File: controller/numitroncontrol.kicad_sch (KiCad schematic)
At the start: 6 parts, among them J1 Conn_01x06, J2 Conn_01x06, J3 Conn_01x06

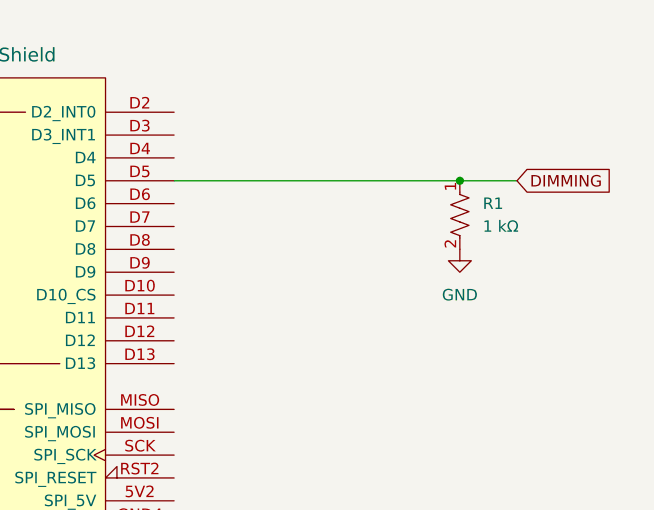
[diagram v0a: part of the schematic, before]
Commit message: arduino pinout
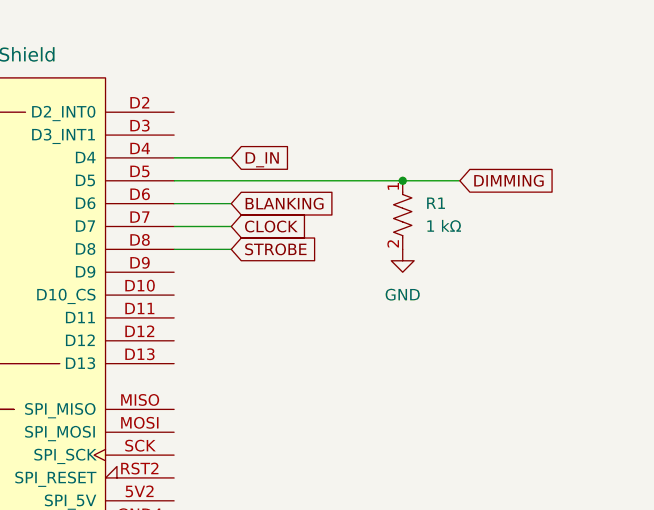
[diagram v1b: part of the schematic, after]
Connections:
- net BLANKING: now also A1.D6
- net CLOCK: now also A1.D7
- net D_IN: now also A1.D4
- net STROBE: now also A1.D8
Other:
- moved on the sheet: R1
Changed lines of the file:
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@@
 	)
 	(junction
-		(at 184.15 44.45)
+		(at 177.8 44.45)
 		(diameter 0)
 		(color 0 0 0 0)
@@
 	(wire
 		(pts
+			(xy 177.8 44.45) (xy 184.15 44.45)
+		)
+		(stroke
+			(width 0)
+			(type default)
+		)
+	)
+	(wire
+		(pts
 			(xy 88.9 90.17) (xy 88.9 87.63)
 		)
@@
 	(wire
 		(pts
+			(xy 158.75 52.07) (xy 152.4 52.07)
+		)
+		(stroke
+			(width 0)
+			(type default)
+		)
+	)
+	(wire
+		(pts
 			(xy 76.2 76.2) (xy 76.2 67.31)
 		)
@@
 	(wire
 		(pts
+			(xy 158.75 49.53) (xy 152.4 49.53)
+		)
+		(stroke
+			(width 0)
+			(type default)
+		)
+	)
+	(wire
+		(pts
 			(xy 157.48 143.51) (xy 161.29 143.51)
 		)
@@
 	(wire
 		(pts
-			(xy 152.4 44.45) (xy 184.15 44.45)
+			(xy 158.75 46.99) (xy 152.4 46.99)
+		)
+		(stroke
+			(width 0)
+			(type default)
+		)
+	)
+	(wire
+		(pts
+			(xy 158.75 41.91) (xy 152.4 41.91)
+		)
+		(stroke
+			(width 0)
+			(type default)
+		)
+	)
+	(wire
+		(pts
+			(xy 152.4 44.45) (xy 177.8 44.45)
 		)
 		(stroke
@@
 		(pts
 			(xy 157.48 148.59) (xy 161.29 148.59)
-		)
-		(stroke
-			(width 0)
-			(type default)
-		)
-	)
-	(wire
-		(pts
-			(xy 190.5 44.45) (xy 184.15 44.45)
 		)
 		(stroke
@@
 		)
 	)
+	(global_label "BLANKING"
+		(shape input)
+		(at 158.75 46.99 0)
+		(fields_autoplaced yes)
+		(effects
+			(font
+				(size 1.27 1.27)
+			)
+			(justify left)
+		)
+		(property "Intersheetrefs" "${INTERSHEET_REFS}"
+			(at 170.9277 46.99 0)
+			(effects
+				(font
+					(size 1.27 1.27)
+				)
+				(justify left)
+				(hide yes)
+			)
+		)
+	)
+	(global_label "STROBE"
+		(shape input)
+		(at 158.75 52.07 0)
+		(fields_autoplaced yes)
+		(effects
+			(font
+				(size 1.27 1.27)
+			)
+			(justify left)
+		)
+		(property "Intersheetrefs" "${INTERSHEET_REFS}"
+			(at 168.9318 52.07 0)
+			(effects
+				(font
+					(size 1.27 1.27)
+				)
+				(justify left)
+				(hide yes)
+			)
+		)
+	)
 	(global_label "STROBE"
 		(shape input)
@@
 	(global_label "CLOCK"
 		(shape input)
+		(at 158.75 49.53 0)
+		(fields_autoplaced yes)
+		(effects
+			(font
+				(size 1.27 1.27)
+			)
+			(justify left)
+		)
+		(property "Intersheetrefs" "${INTERSHEET_REFS}"
+			(at 167.9038 49.53 0)
+			(effects
+				(font
+					(size 1.27 1.27)
+				)
+				(justify left)
+				(hide yes)
+			)
+		)
+	)
+	(global_label "CLOCK"
+		(shape input)
 		(at 97.79 148.59 0)
 		(fields_autoplaced yes)
@@
 	(global_label "DIMMING"
 		(shape input)
-		(at 190.5 44.45 0)
+		(at 184.15 44.45 0)
 		(fields_autoplaced yes)
 		(effects
@@
 		)
 		(property "Intersheetrefs" "${INTERSHEET_REFS}"
-			(at 201.4681 44.45 0)
+			(at 195.1181 44.45 0)
+			(effects
+				(font
+					(size 1.27 1.27)
+				)
+				(justify left)
+				(hide yes)
+			)
+		)
+	)
+	(global_label "D_IN"
+		(shape input)
+		(at 158.75 41.91 0)
+		(fields_autoplaced yes)
+		(effects
+			(font
+				(size 1.27 1.27)
+			)
+			(justify left)
+		)
+		(property "Intersheetrefs" "${INTERSHEET_REFS}"
+			(at 165.9081 41.91 0)
 			(effects
 				(font
@@
 		(lib_name "R_US_2")
 		(lib_id "Device:R_US")
-		(at 184.15 48.26 0)
+		(at 177.8 48.26 0)
 		(unit 1)
 		(exclude_from_sim no)
@@
 		(fields_autoplaced yes)
 		(property "Reference" "R1"
-			(at 186.69 46.9899 0)
+			(at 180.34 46.9899 0)
 			(effects
 				(font
@@
 		)
 		(property "Value" "1 kΩ"
-			(at 186.69 49.5299 0)
+			(at 180.34 49.5299 0)
 			(effects
 				(font
@@
 		)
 		(property "Footprint" "Resistor_SMD:R_1206_3216Metric_Pad1.30x1.75mm_HandSolder"
-			(at 185.166 48.514 90)
+			(at 178.816 48.514 90)
 			(effects
 				(font
@@
 		)
 		(property "Datasheet" "https://www.vishay.com/docs/20035/dcrcwe3.pdf"
-			(at 184.15 48.26 0)
+			(at 177.8 48.26 0)
 			(effects
 				(font
@@
 		)
 		(property "Description" "RES SMD 1K OHM 1% 1/4W 1206"
-			(at 184.15 48.26 0)
+			(at 177.8 48.26 0)
 			(effects
 				(font
@@
 		)
 		(property "MFR" "Vishay Dale"
-			(at 184.15 48.26 0)
+			(at 177.8 48.26 0)
 			(effects
 				(font
@@
 		)
 		(property "Part No" "CRCW040248R7FKED"
-			(at 184.15 48.26 0)
+			(at 177.8 48.26 0)
 			(effects
 				(font
@@
 		)
 		(property "Manufacturer_Name" "Vishay Dale"
-			(at 184.15 48.26 0)
+			(at 177.8 48.26 0)
 			(effects
 				(font
@@
 		)
 		(property "Manufacturer_Part_Number" "CRCW12061K00FKEA"
-			(at 184.15 48.26 0)
+			(at 177.8 48.26 0)
 			(effects
 				(font
@@
 	(symbol
 		(lib_id "power:GND")
-		(at 184.15 52.07 0)
+		(at 177.8 52.07 0)
 		(unit 1)
 		(exclude_from_sim no)
@@
 		(fields_autoplaced yes)
 		(property "Reference" "#PWR09"
-			(at 184.15 58.42 0)
+			(at 177.8 58.42 0)
 			(effects
 				(font
@@
 		)
 		(property "Value" "GND"
-			(at 184.15 57.15 0)
+			(at 177.8 57.15 0)
 			(effects
 				(font
@@
 		)
 		(property "Footprint" ""
-			(at 184.15 52.07 0)
+			(at 177.8 52.07 0)
 			(effects
 				(font
@@
 		)
 		(property "Datasheet" ""
-			(at 184.15 52.07 0)
+			(at 177.8 52.07 0)
 			(effects
 				(font
@@
 		)
 		(property "Description" "Power symbol creates a global label with name \"GND\" , ground"
-			(at 184.15 52.07 0)
-			(effects
-				(font
+			(at 177.8 52.07 0)
+			(effects
+				(font

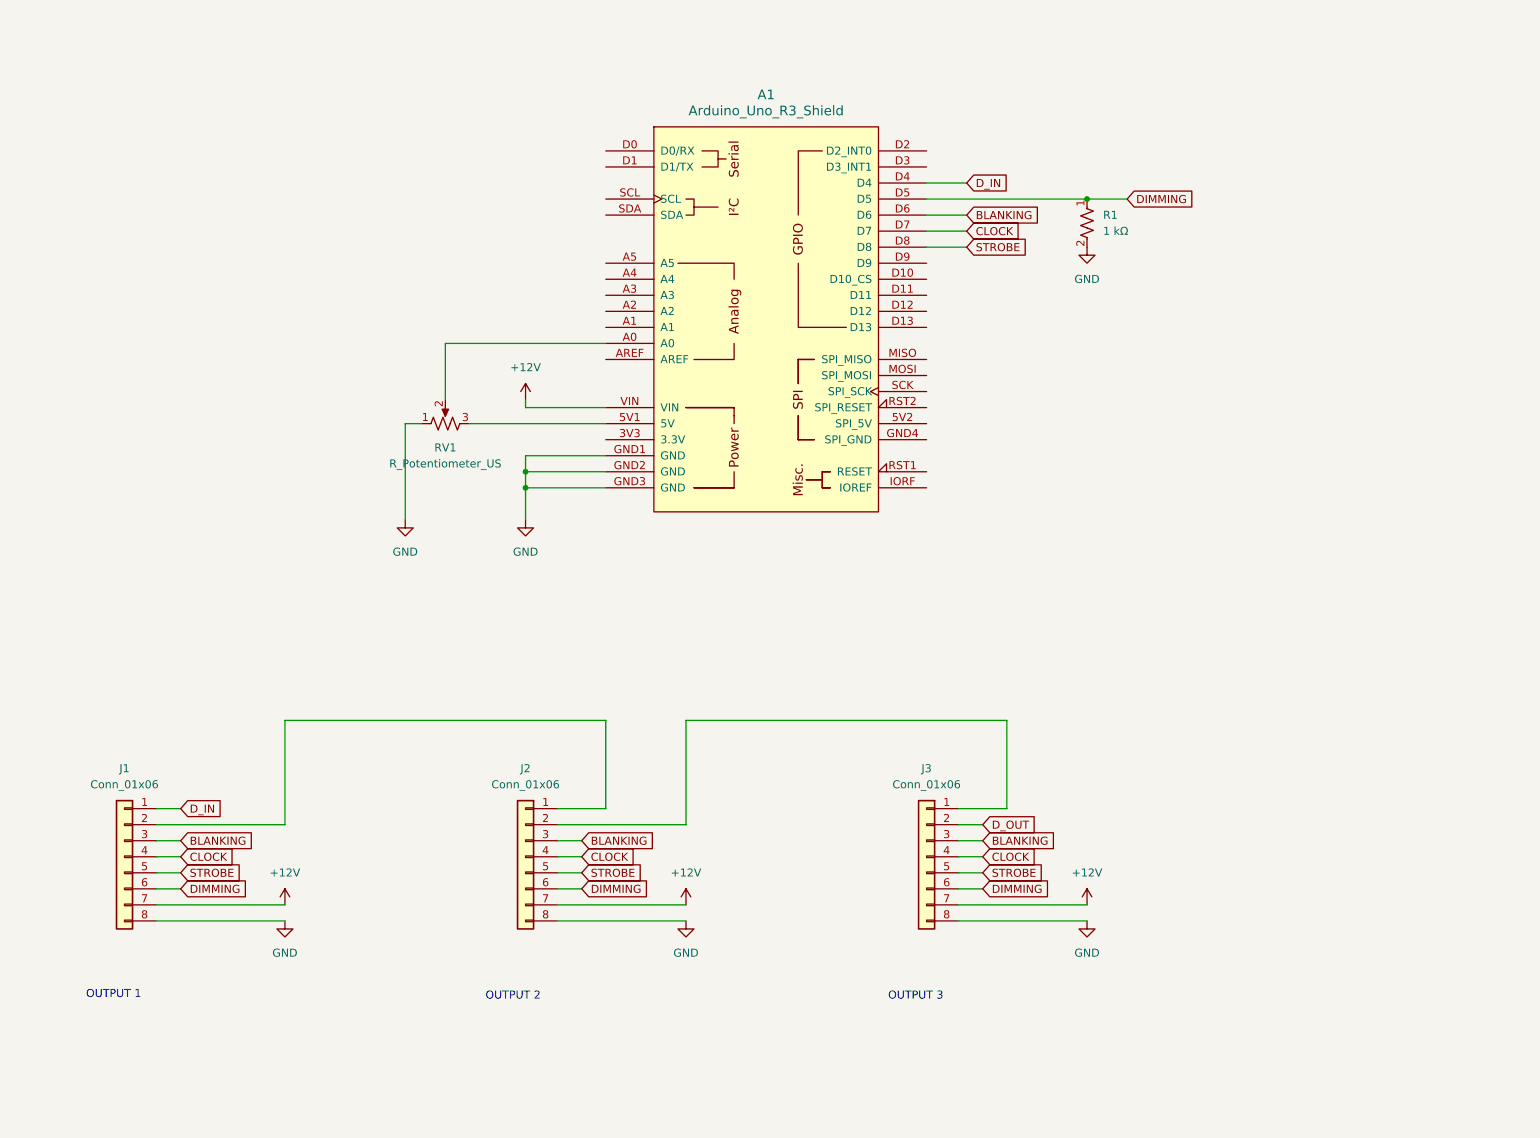
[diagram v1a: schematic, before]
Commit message: continued design work on controller
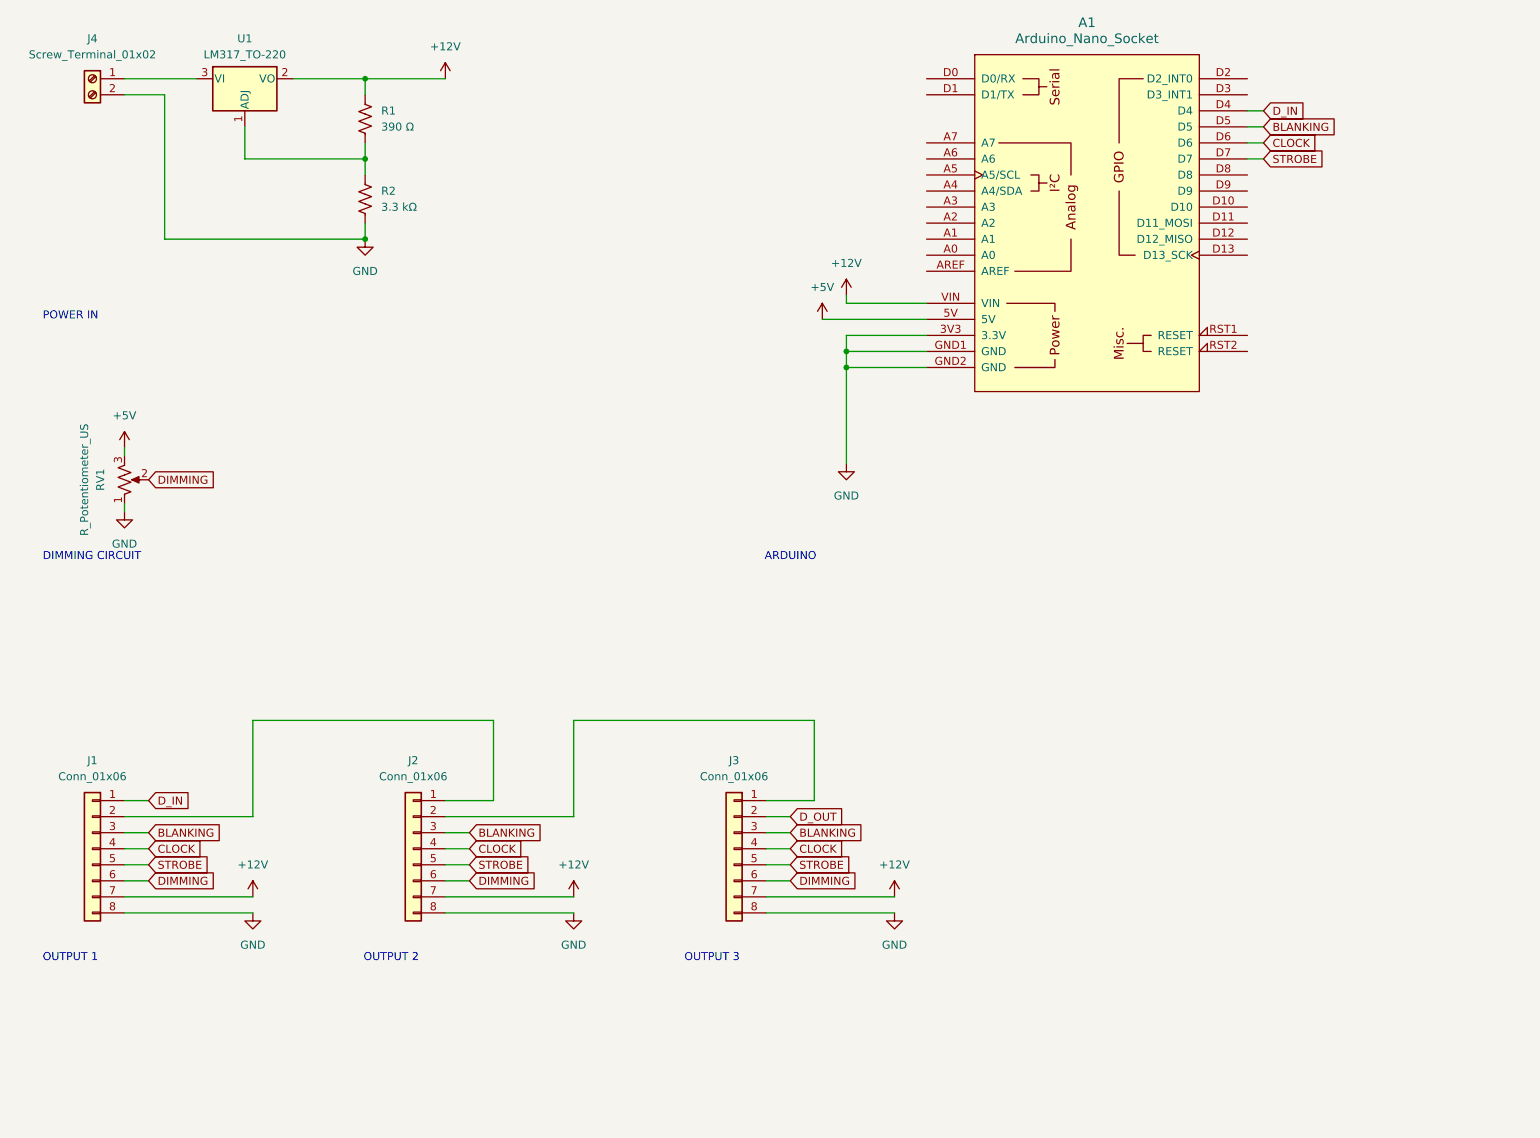
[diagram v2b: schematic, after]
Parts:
- removed A1: Arduino_Uno_R3_Shield, PCM_arduino-library:Arduino_Uno_R3_Shield, symbol PCM_arduino-library:Arduino_Uno_R3_Shield
- added A1: Arduino_Nano_Socket, PCM_arduino-library:Arduino_Nano_Socket, symbol PCM_arduino-library:Arduino_Nano_Socket
- added J4: Screw_Terminal_01x02, symbol Connector:Screw_Terminal_01x02
- added R2: 3.3 kΩ, symbol Device:R_US
- added U1: LM317_TO-220, Package_TO_SOT_THT:TO-220-3_Vertical, symbol Regulator_Linear:LM317_TO-220
- J1, J2, J3: footprint NewFootprints:66100811722 -> Library:61200821621
- R1: value 1 kΩ -> 390 Ω; footprint Resistor_SMD:R_1206_3216Metric_Pad1.30x1.75mm_HandSolder -> (none); MFR Vishay Dale -> (none); Manufacturer_Name Vishay Dale -> (none); Manufacturer_Part_Number CRCW12061K00FKEA -> (none); Part No CRCW040248R7FKED -> (none)
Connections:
- net +12V: now also R1.1, A1.VIN, U1.2 (VO)
- net BLANKING: now also A1.D5
- net CLOCK: now also A1.D6
- net DIMMING: now also RV1.2; no longer R1.1
- net D_IN: now also A1.D4
- net GND: now also A1.3V3 (3.3V), A1.GND1 (GND), A1.GND2 (GND), J4.2 (Pin_2), R2.2; no longer R1.2
- net STROBE: now also A1.D7
- net +5V: now reaches RV1.3
- net +5V: now also A1.5V
- new net: R1.2, R2.1, U1.1 (ADJ)
- new net: J4.1 (Pin_1), U1.3 (VI)
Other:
- note added: "ARDUINO"
- note added: "DIMMING CIRCUIT"
- note added: "POWER IN"
- moved on the sheet: J1, J2, J3, RV1

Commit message: finished controller schematic, started pcb
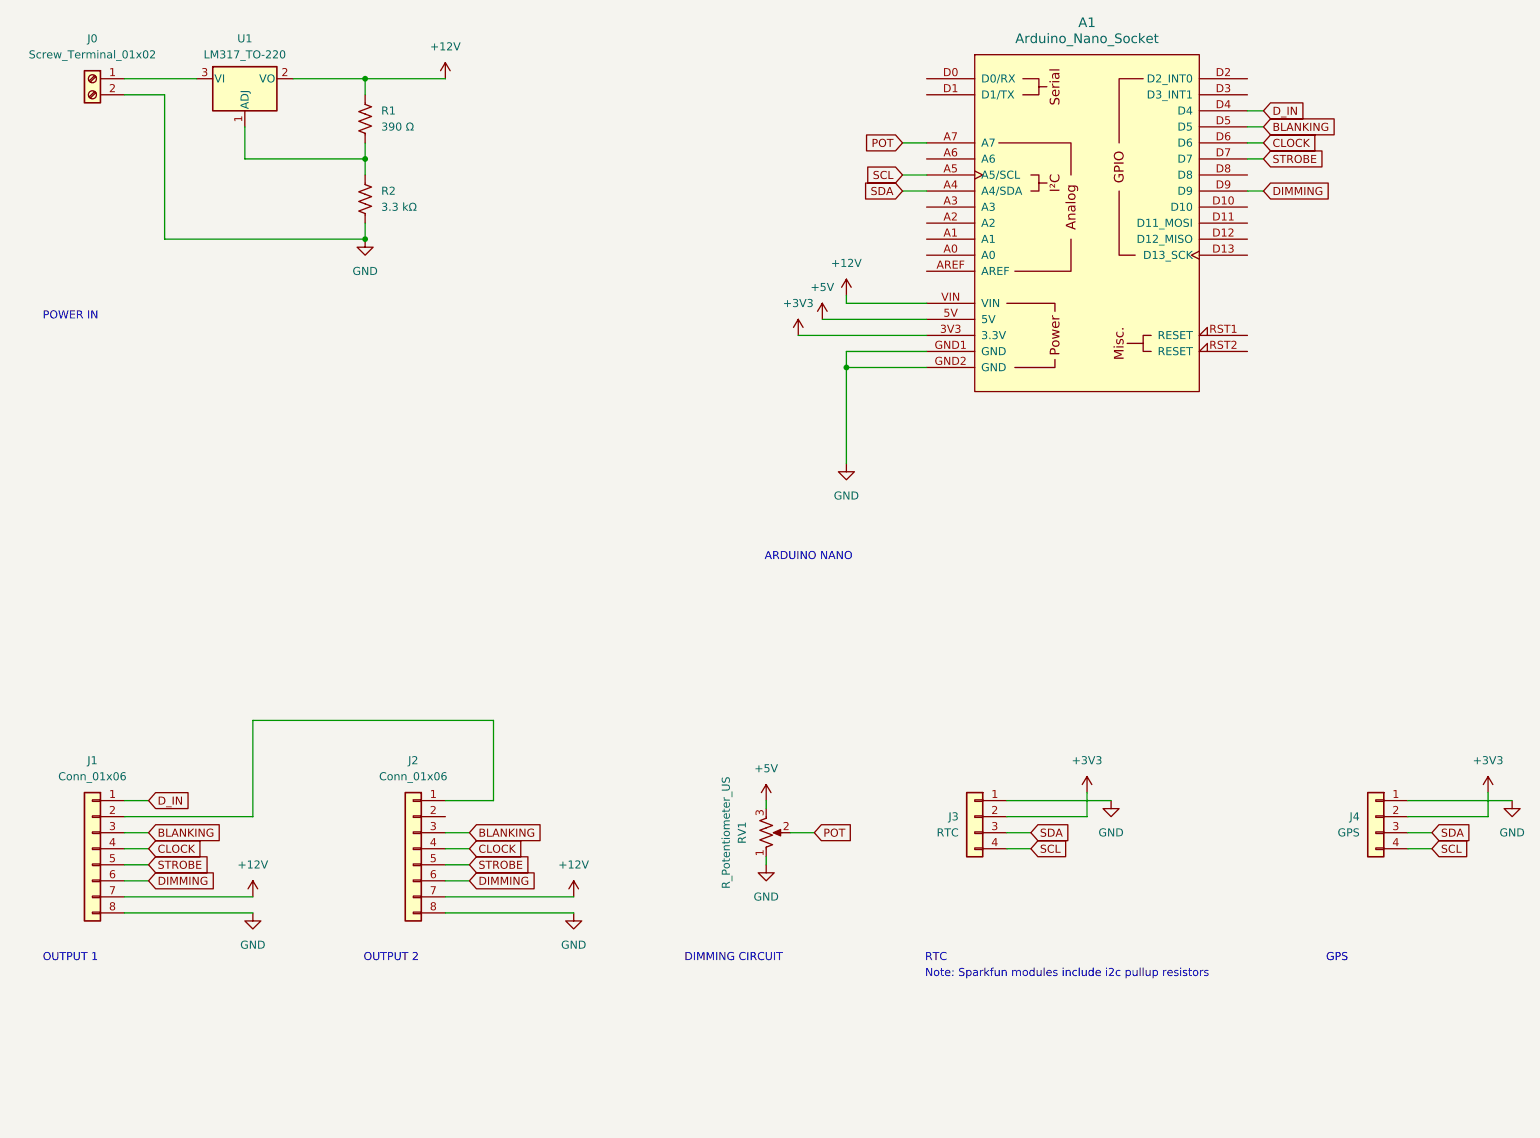
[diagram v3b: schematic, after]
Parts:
- removed J3: Conn_01x06, Library:61200821621, symbol Connector_Generic:Conn_01x08
- added J3: RTC, Connector_PinHeader_2.54mm:PinHeader_1x04_P2.54mm_Vertical, symbol Connector_Generic:Conn_01x04
- added J4: GPS, Connector_PinHeader_2.54mm:PinHeader_1x04_P2.54mm_Vertical, symbol Connector_Generic:Conn_01x04
- J0: renamed from J4; footprint (none) -> TerminalBlock_4Ucon:TerminalBlock_4Ucon_1x02_P3.50mm_Horizontal
- R1, R2: footprint (none) -> Resistor_SMD:R_0805_2012Metric_Pad1.20x1.40mm_HandSolder
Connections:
- net DIMMING: now also A1.D9; no longer RV1.2
- net GND: now also J3.1 (Pin_1), J4.1 (Pin_1); no longer A1.3V3 (3.3V)
- net SDA: now reaches A1.A4 (A4/SDA)
- net SDA: now also J3.3 (Pin_3), J4.3 (Pin_3)
- net SCL: now reaches A1.A5 (A5/SCL)
- net SCL: now also J3.4 (Pin_4), J4.4 (Pin_4)
- net POT: now reaches A1.A7
- net POT: now also RV1.2
- new net +3V3: A1.3V3 (3.3V), J3.2 (Pin_2), J4.2 (Pin_2)
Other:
- note added: "ARDUINO NANO"
- note added: "GPS"
- note added: "Note: Sparkfun modules include i2c pullup resistors"
- note added: "RTC"
- note removed: "ARDUINO"
- note removed: "OUTPUT 3"
- moved on the sheet: RV1

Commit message: played tetris on pcb and re-exported prod files
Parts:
- RV1: footprint (none) -> Connector_PinHeader_2.54mm:PinHeader_1x03_P2.54mm_Vertical
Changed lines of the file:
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@@
 			)
 		)
-		(property "Footprint" ""
+		(property "Footprint" "Connector_PinHeader_2.54mm:PinHeader_1x03_P2.54mm_Vertical"
 			(at 127 144.78 0)
 			(effects
